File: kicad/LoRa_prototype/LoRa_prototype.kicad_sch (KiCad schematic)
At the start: 0 parts

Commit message: Prettified schematic
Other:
- sheet GPS renamed GPS AND GAS SENSORS
- sheet Power management renamed POWER
- sheet Programming interface renamed PROGRAMMING
- sheet RF Switch + Antenna renamed ANTENNA
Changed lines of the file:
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@@
 		(on_board yes)
 		(dnp no)
-		(fields_autoplaced yes)
-		(stroke
-			(width 0.1524)
-			(type solid)
-		)
-		(fill
-			(color 212 212 212 1.0000)
-		)
-		(property "Sheetname" "GPS"
-			(at 179.07 107.2384 0)
-			(effects
-				(font
-					(size 1.27 1.27)
+		(stroke
+			(width 0.1524)
+			(type solid)
+		)
+		(fill
+			(color 212 212 212 1.0000)
+		)
+		(property "Sheetname" "GPS AND GAS SENSORS"
+			(at 169.418 145.034 0)
+			(effects
+				(font
+					(size 2.54 2.54)
+					(thickness 0.508)
+					(bold yes)
 				)
 				(justify left bottom)
@@
 	)
 	(sheet
-		(at 83.82 99.06)
-		(size 17.78 25.4)
+		(at 85.09 99.06)
+		(size 16.51 25.4)
 		(exclude_from_sim no)
 		(in_bom yes)
 		(on_board yes)
 		(dnp no)
-		(fields_autoplaced yes)
-		(stroke
-			(width 0.1524)
-			(type solid)
-		)
-		(fill
-			(color 212 212 212 1.0000)
-		)
-		(property "Sheetname" "Power management"
-			(at 83.82 98.3484 0)
-			(effects
-				(font
-					(size 1.27 1.27)
+		(stroke
+			(width 0.1524)
+			(type solid)
+		)
+		(fill
+			(color 212 212 212 1.0000)
+		)
+		(property "Sheetname" "POWER"
+			(at 85.852 98.552 0)
+			(effects
+				(font
+					(size 2.54 2.54)
+					(thickness 0.508)
+					(bold yes)
 				)
 				(justify left bottom)
@@
 		)
 		(property "Sheetfile" "power.kicad_sch"
-			(at 83.82 125.0446 0)
+			(at 85.09 125.0446 0)
 			(effects
 				(font
@@
 	(sheet
 		(at 179.07 69.85)
-		(size 24.13 34.29)
+		(size 35.56 34.29)
 		(exclude_from_sim no)
 		(in_bom yes)
@@
 			(color 212 212 212 1.0000)
 		)
-		(property "Sheetname" "RF Switch + Antenna"
-			(at 179.07 69.1384 0)
-			(effects
-				(font
-					(size 1.27 1.27)
+		(property "Sheetname" "ANTENNA"
+			(at 179.07 68.5034 0)
+			(effects
+				(font
+					(size 2.54 2.54)
+					(thickness 0.508)
+					(bold yes)
 				)
 				(justify left bottom)
@@
 	)
 	(sheet
-		(at 87.63 69.85)
-		(size 13.97 24.13)
+		(at 77.47 69.85)
+		(size 24.13 24.13)
 		(exclude_from_sim no)
 		(in_bom yes)
@@
 			(color 212 212 212 1.0000)
 		)
-		(property "Sheetname" "Programming interface"
-			(at 84.836 69.342 0)
-			(effects
-				(font
-					(size 1.27 1.27)
+		(property "Sheetname" "PROGRAMMING"
+			(at 75.692 69.088 0)
+			(effects
+				(font
+					(size 2.54 2.54)
+					(thickness 0.508)
+					(bold yes)
 				)
 				(justify left bottom)
@@
 		)
 		(property "Sheetfile" "programming_interface.kicad_sch"
-			(at 87.63 94.5646 0)
+			(at 77.47 94.5646 0)
 			(effects
 				(font
@@
 		)
 		(property "Sheetname" "MCU"
-			(at 123.19 69.1384 0)
-			(effects
-				(font
-					(size 1.27 1.27)
-				)
-				(justify left bottom)
+			(at 123.19 68.5034 0)
+			(effects
+				(font
+					(size 2.54 2.54)
+					(thickness 0.508)
+					(bold yes)
+				)
+				(justify left bottom)

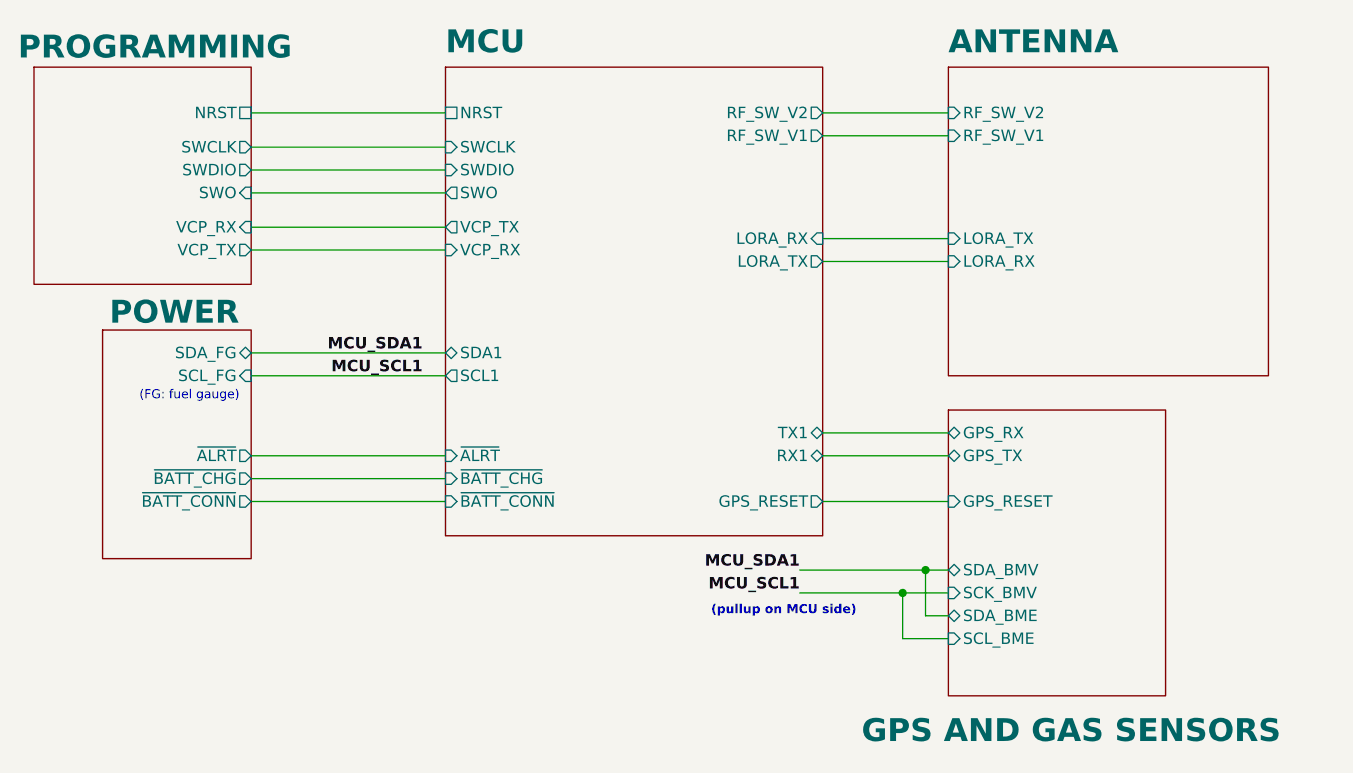
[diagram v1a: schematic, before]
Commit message: Added pin headers in schematics
To activate/deactivate subsystems as well as measure currents
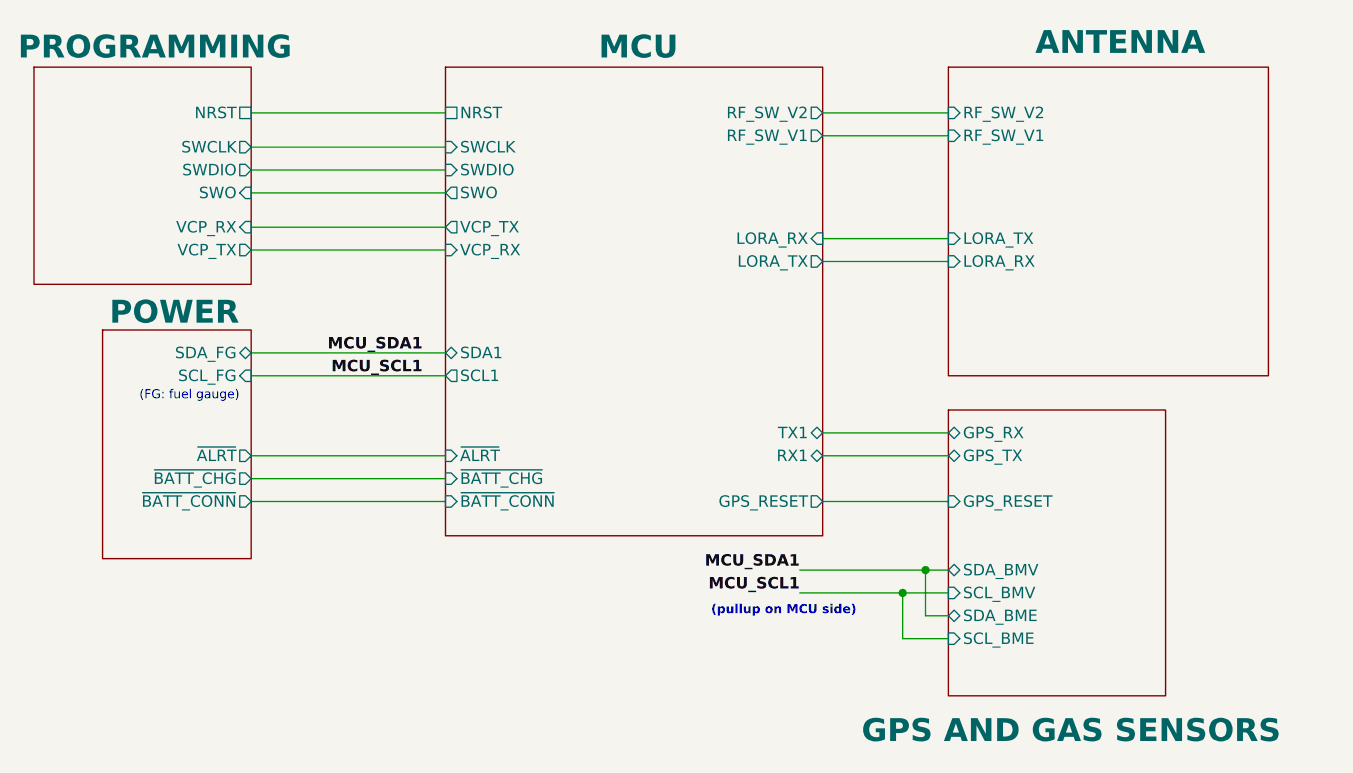
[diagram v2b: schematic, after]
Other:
- sheet GPS AND GAS SENSORS ports: added SCL_BMV; removed SCK_BMV
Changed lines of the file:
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@@
 			)
 		)
-		(pin "SCK_BMV" input
+		(pin "SCL_BMV" input
 			(at 179.07 128.27 180)
 			(effects
@@
 		(on_board yes)
 		(dnp no)
-		(fields_autoplaced yes)
 		(stroke
 			(width 0.1524)
@@
 		)
 		(property "Sheetname" "ANTENNA"
-			(at 179.07 68.5034 0)
+			(at 188.722 68.58 0)
 			(effects
 				(font
@@
 		(on_board yes)
 		(dnp no)
-		(fields_autoplaced yes)
 		(stroke
 			(width 0.1524)
@@
 		)
 		(property "Sheetname" "MCU"
-			(at 123.19 68.5034 0)
-			(effects
-				(font
+			(at 140.208 69.088 0)
+			(effects
+				(font

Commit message: 90% done (before ground and power pour)
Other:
- sheet MCU ports: added none; removed ~{BATT_CHG}, ~{BATT_CONN}
- sheet POWER ports: added none; removed ~{BATT_CHG}, ~{BATT_CONN}
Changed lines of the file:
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@@
-	(wire
-		(pts
-			(xy 101.6 115.57) (xy 123.19 115.57)
-		)
-		(stroke
-			(width 0)
-			(type default)
-		)
-	)
 	(wire
 		(pts
@@
 		(pts
 			(xy 101.6 81.28) (xy 123.19 81.28)
-		)
-		(stroke
-			(width 0)
-			(type default)
-		)
-	)
-	(wire
-		(pts
-			(xy 101.6 118.11) (xy 123.19 118.11)
 		)
 		(stroke
@@
 			)
 		)
-		(pin "~{BATT_CHG}" output
-			(at 101.6 115.57 0)
-			(effects
-				(font
-					(size 1.27 1.27)
-				)
-				(justify right)
-			)
-		)
-		(pin "~{BATT_CONN}" output
-			(at 101.6 118.11 0)
-			(effects
-				(font
-					(size 1.27 1.27)
-				)
-				(justify right)
-			)
-		)
 		(pin "SDA_FG" bidirectional
 			(at 101.6 101.6 0)
@@
 			)
 		)
-		(pin "~{BATT_CONN}" input
-			(at 123.19 118.11 180)
-			(effects
-				(font
-					(size 1.27 1.27)
-				)
-				(justify left)
-			)
-		)
 		(pin "~{ALRT}" input
 			(at 123.19 113.03 180)
 			(effects
 				(font
-					(size 1.27 1.27)
-				)
-				(justify left)
-			)
-		)
-		(pin "~{BATT_CHG}" input
-			(at 123.19 115.57 180)
-			(effects
-				(font
